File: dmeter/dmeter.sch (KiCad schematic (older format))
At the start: 104 parts, among them J1 INPUT, Q1 BC556, Q2 BC556, Q3 BC556, Q4 BC556, Q5 BC556, U1 TL072, U10 LM339, U2 TL072, U3 TL072, U4 TL072, U5 LM339, U6 LM339, U7 LM339, U8 LM339, U9 LM339

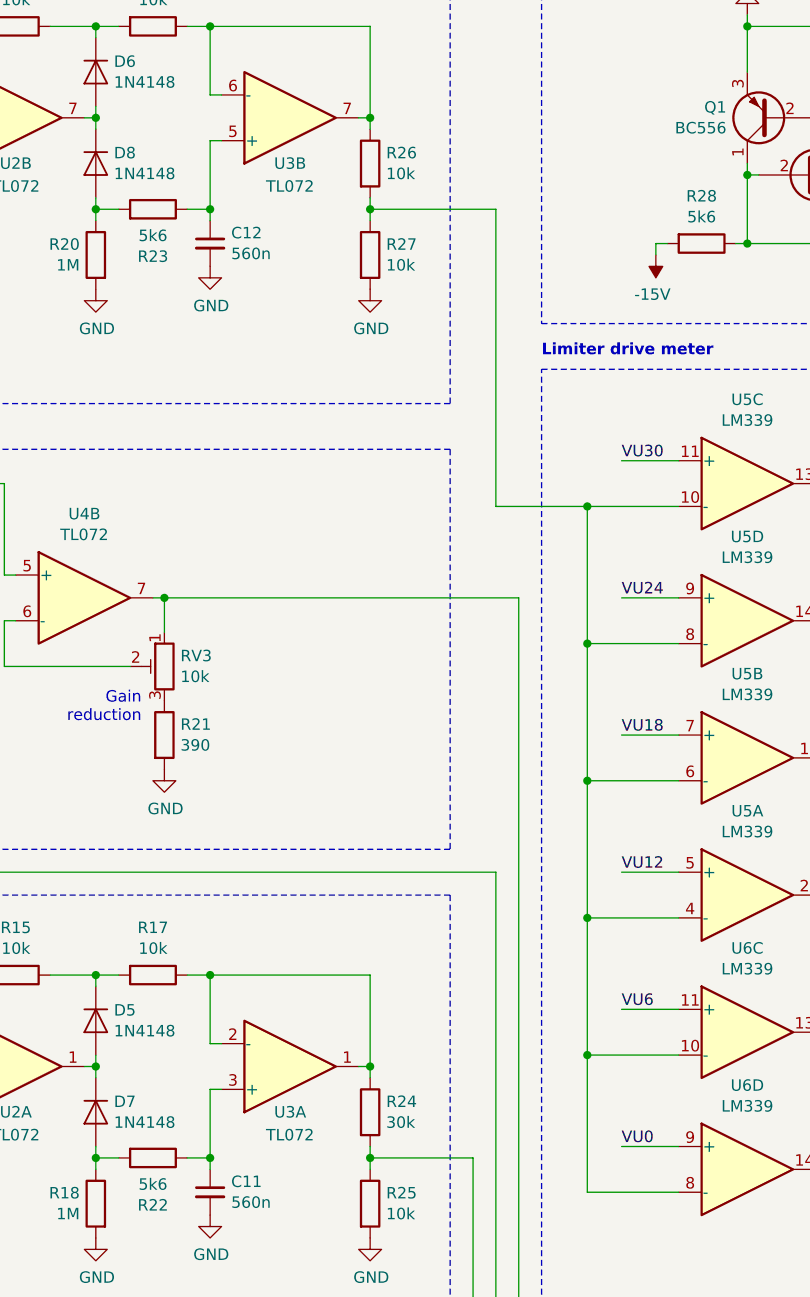
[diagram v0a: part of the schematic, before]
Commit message: Change R24 to 10k, R26 to 30k to correct input/output meter reference levels
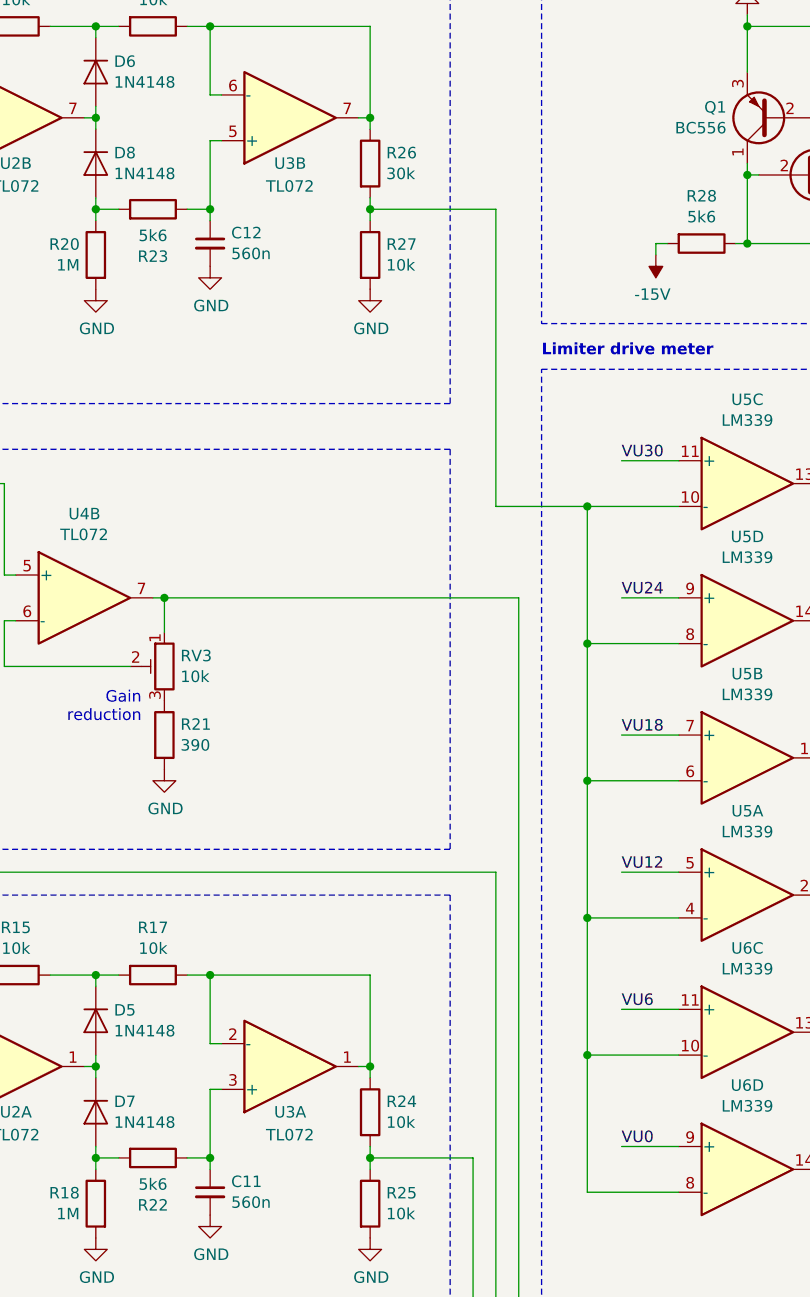
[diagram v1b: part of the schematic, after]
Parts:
- R24: value 30k -> 10k
- R26: value 10k -> 30k
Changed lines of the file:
@@
 P 7250 6500
 F 0 "R24" H 7320 6546 50  0000 L CNN
-F 1 "30k" H 7320 6455 50  0000 L CNN
+F 1 "10k" H 7320 6455 50  0000 L CNN
 F 2 "amproc:R_Axial_DIN0207_L6.3mm_D2.5mm_P7.62mm_Horizontal_FabText" V 7180 6500 50  0001 C CNN
 F 3 "~" H 7250 6500 50  0001 C CNN
@@
 P 7250 2350
 F 0 "R26" H 7320 2396 50  0000 L CNN
-F 1 "10k" H 7320 2305 50  0000 L CNN
+F 1 "30k" H 7320 2305 50  0000 L CNN
 F 2 "amproc:R_Axial_DIN0207_L6.3mm_D2.5mm_P7.62mm_Horizontal_FabText" V 7180 2350 50  0001 C CNN
 F 3 "~" H 7250 2350 50  0001 C CNN
